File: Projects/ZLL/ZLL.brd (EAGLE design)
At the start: 34.5 x 25.8 mm, 18 parts, among them IC1 BMD-340-A-R, U1 BSS138BKW, X1 USB-MICROB, Y3 32.768kHz

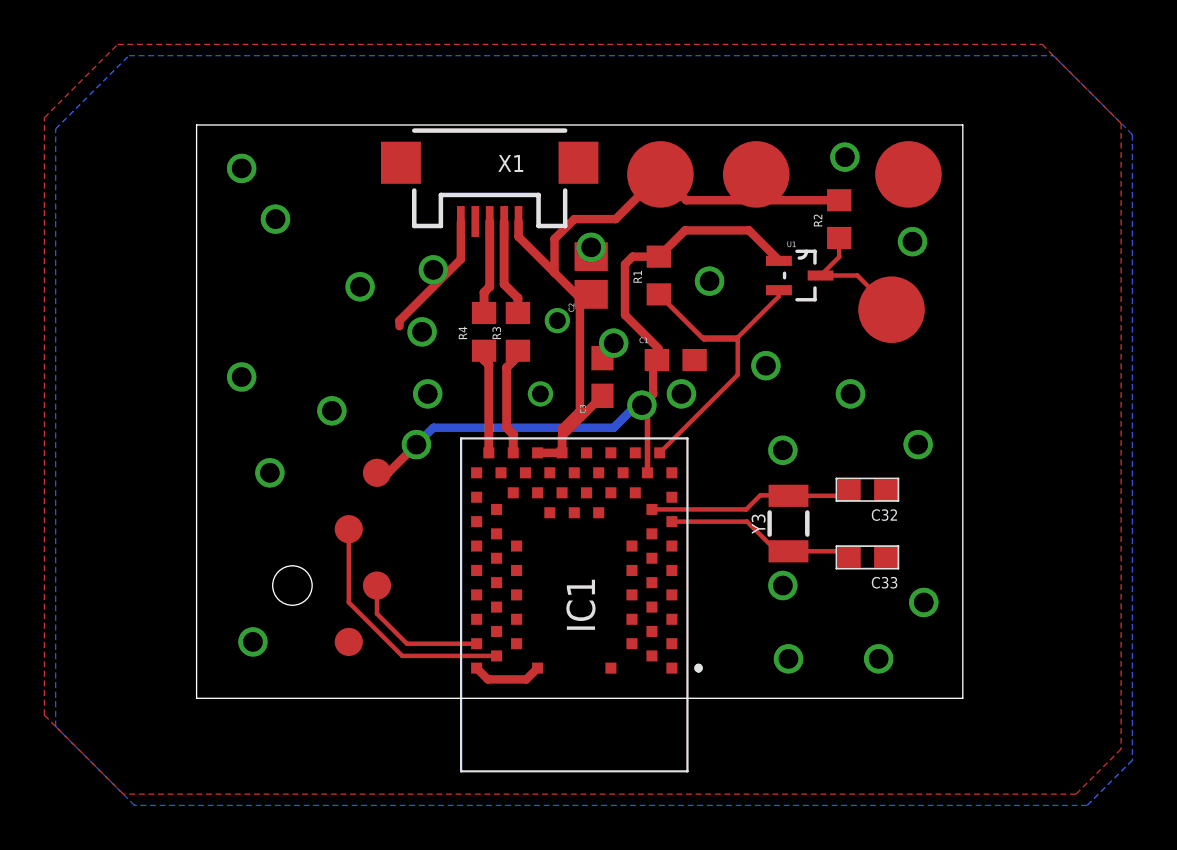
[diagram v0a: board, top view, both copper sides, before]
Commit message: Added buttons on ZLL Added pads on nRF51 key SD prog finished N5 lib updated
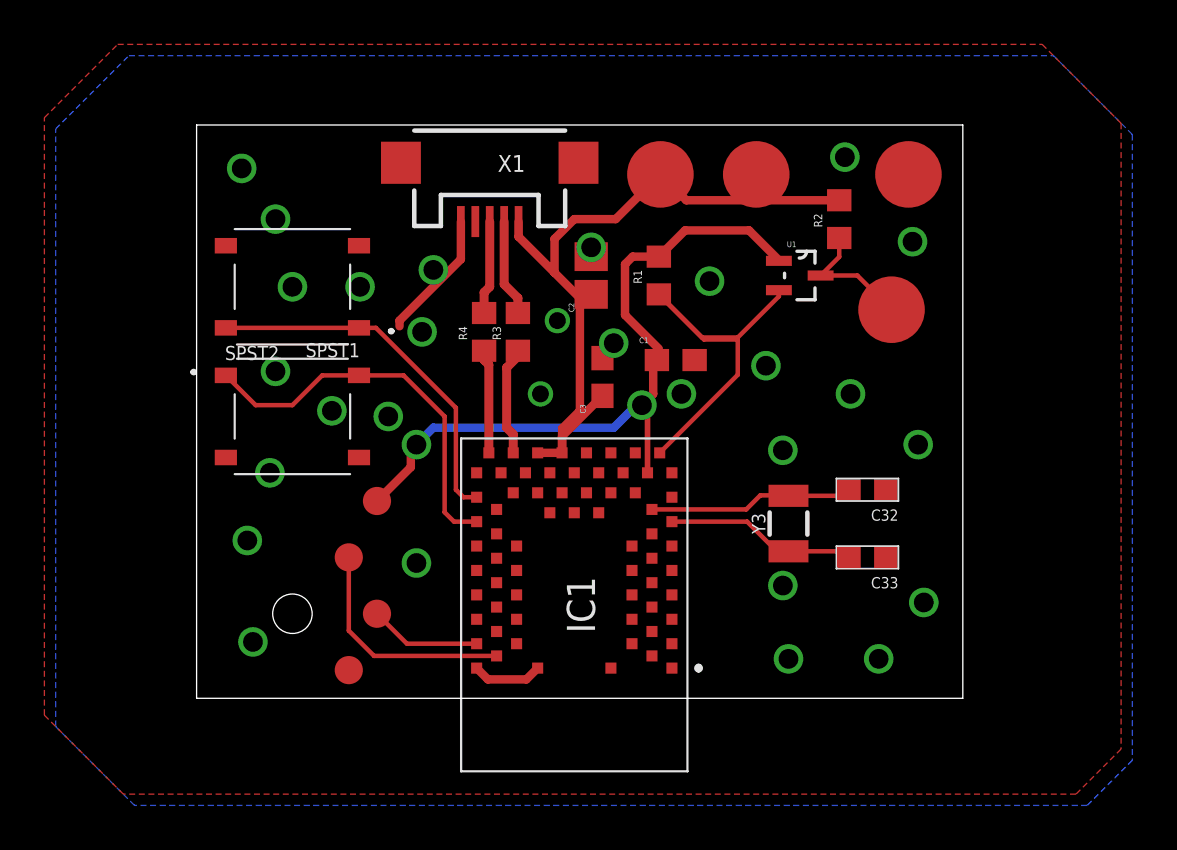
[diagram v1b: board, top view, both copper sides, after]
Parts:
- added SPST1, SPST2: PTS526SK08, SPST:PTS526SKG15SMTR2LFS
- moved U$1 1.27 mm to (8.89, 5.08)
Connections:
- new net SPST1: IC1.31, SPST1.1, SPST1.2
- new net SPST2: IC1.33, SPST2.1, SPST2.2
- net GND: now also SPST1.3, SPST1.4, SPST2.3, SPST2.4
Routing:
- net SPST2: track 0.00 -> 17.7 mm
- net SPST1: track 0.00 -> 16.6 mm
- net IC1_SWCLK: track 6.32 -> 5.05 mm
- net IC1_VCC: track 31.7 -> 32.6 mm
- net IC1_SWDIO: track 11.0 -> 10.4 mm
- net GND: vias 26 -> 29
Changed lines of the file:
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@@
 <attribute name="VALUE" x="32.131" y="20.066" size="0.381" layer="27" rot="R90"/>
 </element>
-<element name="U$1" library="Prog" package="PROG_SMD" value="PROG_SMD" x="8.89" y="6.35" smashed="yes" rot="R270"/>
+<element name="U$1" library="Prog" package="PROG_SMD" value="PROG_SMD" x="8.89" y="5.08" smashed="yes" rot="R270"/>
 <element name="U1" library="BSS138" package="SOT65P210X110-3N" value="BSS138BKW" x="29.21" y="19.05" smashed="yes">
 <attribute name="MPN" value="BSS138BKW" x="44.45" y="-5.08" size="1.778" layer="27" display="off"/>
@@
 <element name="5V1" library="Exposed_pad" package="PAD_3" value="PAD3MM" x="26.924" y="22.606" smashed="yes"/>
 <element name="NEO_HV1" library="Exposed_pad" package="PAD_3" value="PAD3MM" x="33.782" y="22.606" smashed="yes"/>
+<element name="SPST1" library="SPST" package="PTS526SKG15SMTR2LFS" value="PTS526SK08" x="6.35" y="18.542" smashed="yes" rot="R180">
+<attribute name="MTN" value="611-PTS526SK08SMTR2L" x="6.35" y="18.542" size="1.778" layer="27" rot="R180" display="off"/>
+<attribute name="NAME" x="9.39" y="16.002" size="0.635" layer="25" rot="R180"/>
+<attribute name="VALUE" x="9.39" y="21.082" size="0.635" layer="27" rot="R180" align="top-left"/>
+</element>
+<element name="SPST2" library="SPST" package="PTS526SKG15SMTR2LFS" value="PTS526SK08" x="6.35" y="12.7" smashed="yes">
+<attribute name="MTN" value="611-PTS526SK08SMTR2L" x="6.35" y="12.7" size="1.778" layer="27" display="off"/>
+<attribute name="NAME" x="3.31" y="15.24" size="0.635" layer="25"/>
+<attribute name="VALUE" x="3.31" y="10.16" size="0.635" layer="27" align="top-left"/>
+</element>
 </elements>
 <signals>
@@
 <wire x1="21.336" y1="19.558" x2="21.678" y2="19.9" width="0.381" layer="1"/>
 <wire x1="21.678" y1="19.9" x2="22.86" y2="19.9" width="0.381" layer="1"/>
-<wire x1="10.16" y1="10.16" x2="10.668" y2="10.16" width="0.381" layer="1"/>
-<wire x1="10.668" y1="10.16" x2="11.938" y2="11.43" width="0.381" layer="1"/>
+<wire x1="11.684" y1="11.176" x2="11.684" y2="10.414" width="0.381" layer="1"/>
+<wire x1="10.16" y1="8.89" x2="11.684" y2="10.414" width="0.381" layer="1"/>
+<wire x1="11.684" y1="11.176" x2="11.938" y2="11.43" width="0.381" layer="1"/>
 <via x="11.938" y="11.43" extent="1-16" drill="0.889"/>
 <wire x1="11.938" y1="11.43" x2="12.7" y2="12.192" width="0.381" layer="16"/>
@@
 <wire x1="14.65" y1="2.46" x2="11.51" y2="2.46" width="0.2032" layer="1"/>
 <wire x1="11.51" y1="2.46" x2="10.16" y2="3.81" width="0.2032" layer="1"/>
-<wire x1="10.16" y1="3.81" x2="10.16" y2="5.08" width="0.2032" layer="1"/>
 </signal>
 <signal name="IC1_SWDIO" class="3">
 <contactref element="IC1" pad="44"/>
 <contactref element="U$1" pad="PIN2"/>
-<wire x1="15.55" y1="1.91" x2="11.298" y2="1.91" width="0.2032" layer="1"/>
-<wire x1="11.298" y1="1.91" x2="8.89" y2="4.318" width="0.2032" layer="1"/>
-<wire x1="8.89" y1="4.318" x2="8.89" y2="7.62" width="0.2032" layer="1"/>
+<wire x1="15.55" y1="1.91" x2="10.028" y2="1.91" width="0.2032" layer="1"/>
+<wire x1="10.028" y1="1.91" x2="8.89" y2="3.048" width="0.2032" layer="1"/>
+<wire x1="8.89" y1="3.048" x2="8.89" y2="6.35" width="0.2032" layer="1"/>
 </signal>
 <signal name="IC1_USB-D-" class="2">
@@
 <via x="5.588" y="21.59" extent="1-16" drill="0.889"/>
 <via x="9.398" y="18.542" extent="1-16" drill="0.889"/>
-<via x="4.064" y="14.478" extent="1-16" drill="0.889"/>
+<via x="5.588" y="14.732" extent="1-16" drill="0.889"/>
 <via x="8.128" y="12.954" extent="1-16" drill="0.889"/>
 <via x="5.334" y="10.16" extent="1-16" drill="0.889"/>
@@
 <via x="20.828" y="16.002" extent="1-16" drill="0.889"/>
 <via x="4.064" y="23.876" extent="1-16" drill="0.889"/>
-<via x="12.446" y="13.716" extent="1-16" drill="0.889"/>
+<via x="10.668" y="12.7" extent="1-16" drill="0.889"/>
 <via x="12.192" y="16.51" extent="1-16" drill="0.889"/>
 <via x="12.7" y="19.304" extent="1-16" drill="0.889"/>
@@
 <wire x1="16.892" y1="0.852" x2="17.4" y2="1.36" width="0.381" layer="1"/>
 <contactref element="NEO_HV1" pad="P$1"/>
+<contactref element="SPST1" pad="4"/>
+<contactref element="SPST1" pad="3"/>
+<contactref element="SPST2" pad="4"/>
+<contactref element="SPST2" pad="3"/>
+<via x="6.35" y="18.542" extent="1-16" drill="0.889"/>
+<via x="11.938" y="6.096" extent="1-16" drill="0.889"/>
+<via x="4.318" y="7.112" extent="1-16" drill="0.889"/>
 <wire x1="14.65" y1="10.16" x2="15.75" y2="10.16" width="0" layer="19" extent="1-1"/>
+<wire x1="17.95" y1="8.36" x2="15.75" y2="10.16" width="0" layer="19" extent="1-1"/>
 </signal>
 <signal name="NEO_HV">
@@
 <wire x1="31.134" y1="9.124" x2="31.408" y2="9.398" width="0.2032" layer="1"/>
 </signal>
+<signal name="SPST1">
+<contactref element="SPST1" pad="2"/>
+<contactref element="SPST1" pad="1"/>
+<contactref element="IC1" pad="31"/>
+<wire x1="9.35" y1="16.692" x2="10.112" y2="16.692" width="0.2032" layer="1"/>
+<wire x1="13.716" y1="13.088" x2="10.112" y2="16.692" width="0.2032" layer="1"/>
+<wire x1="14.054" y1="9.06" x2="14.65" y2="9.06" width="0.2032" layer="1"/>
+<wire x1="13.716" y1="13.088" x2="13.716" y2="9.398" width="0.2032" layer="1"/>
+<wire x1="13.716" y1="9.398" x2="14.054" y2="9.06" width="0.2032" layer="1"/>
+<wire x1="3.35" y1="16.692" x2="9.35" y2="16.692" width="0.2032" layer="1"/>
+</signal>
+<signal name="SPST2">
+<contactref element="SPST2" pad="2"/>
+<contactref element="SPST2" pad="1"/>
+<contactref element="IC1" pad="33"/>
+<wire x1="9.35" y1="14.55" x2="11.358" y2="14.55" width="0.2032" layer="1"/>
+<wire x1="13.208" y1="8.382" x2="13.63" y2="7.96" width="0.2032" layer="1"/>
+<wire x1="13.63" y1="7.96" x2="14.65" y2="7.96" width="0.2032" layer="1"/>
+<wire x1="11.358" y1="14.55" x2="13.208" y2="12.7" width="0.2032" layer="1"/>
+<wire x1="13.208" y1="12.7" x2="13.208" y2="8.382" width="0.2032" layer="1"/>
+<wire x1="3.35" y1="14.55" x2="4.692" y2="13.208" width="0.2032" layer="1"/>
+<wire x1="7.692" y1="14.55" x2="9.35" y2="14.55" width="0.2032" layer="1"/>
+<wire x1="4.692" y1="13.208" x2="6.35" y2="13.208" width="0.2032" layer="1"/>
+<wire x1="6.35" y1="13.208" x2="7.692" y2="14.55" width="0.2032" layer="1"/>
+</signal>
 </signals>

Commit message: Order @ Boktech
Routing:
- net GND: track 9.03 -> 10.1 mm, vias 29 -> 33
